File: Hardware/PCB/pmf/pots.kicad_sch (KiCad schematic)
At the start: 39 parts, among them U3 TL074, U4 TL072

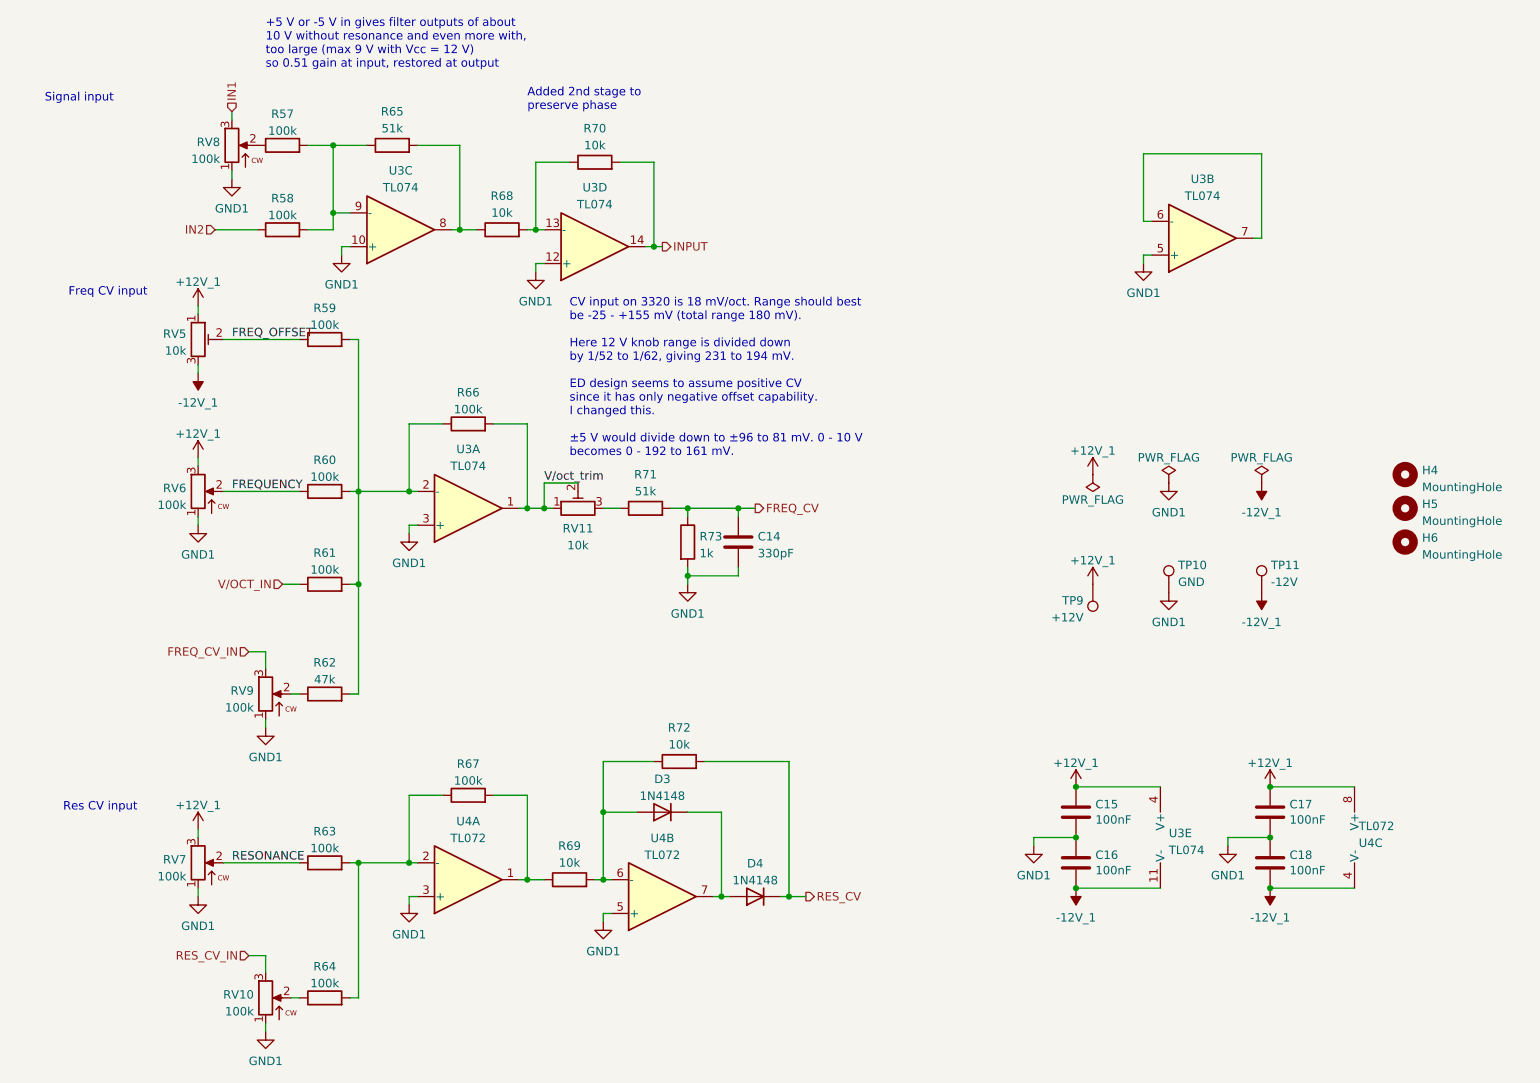
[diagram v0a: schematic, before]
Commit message: CVf test point; disambiguate heirarchical symbols
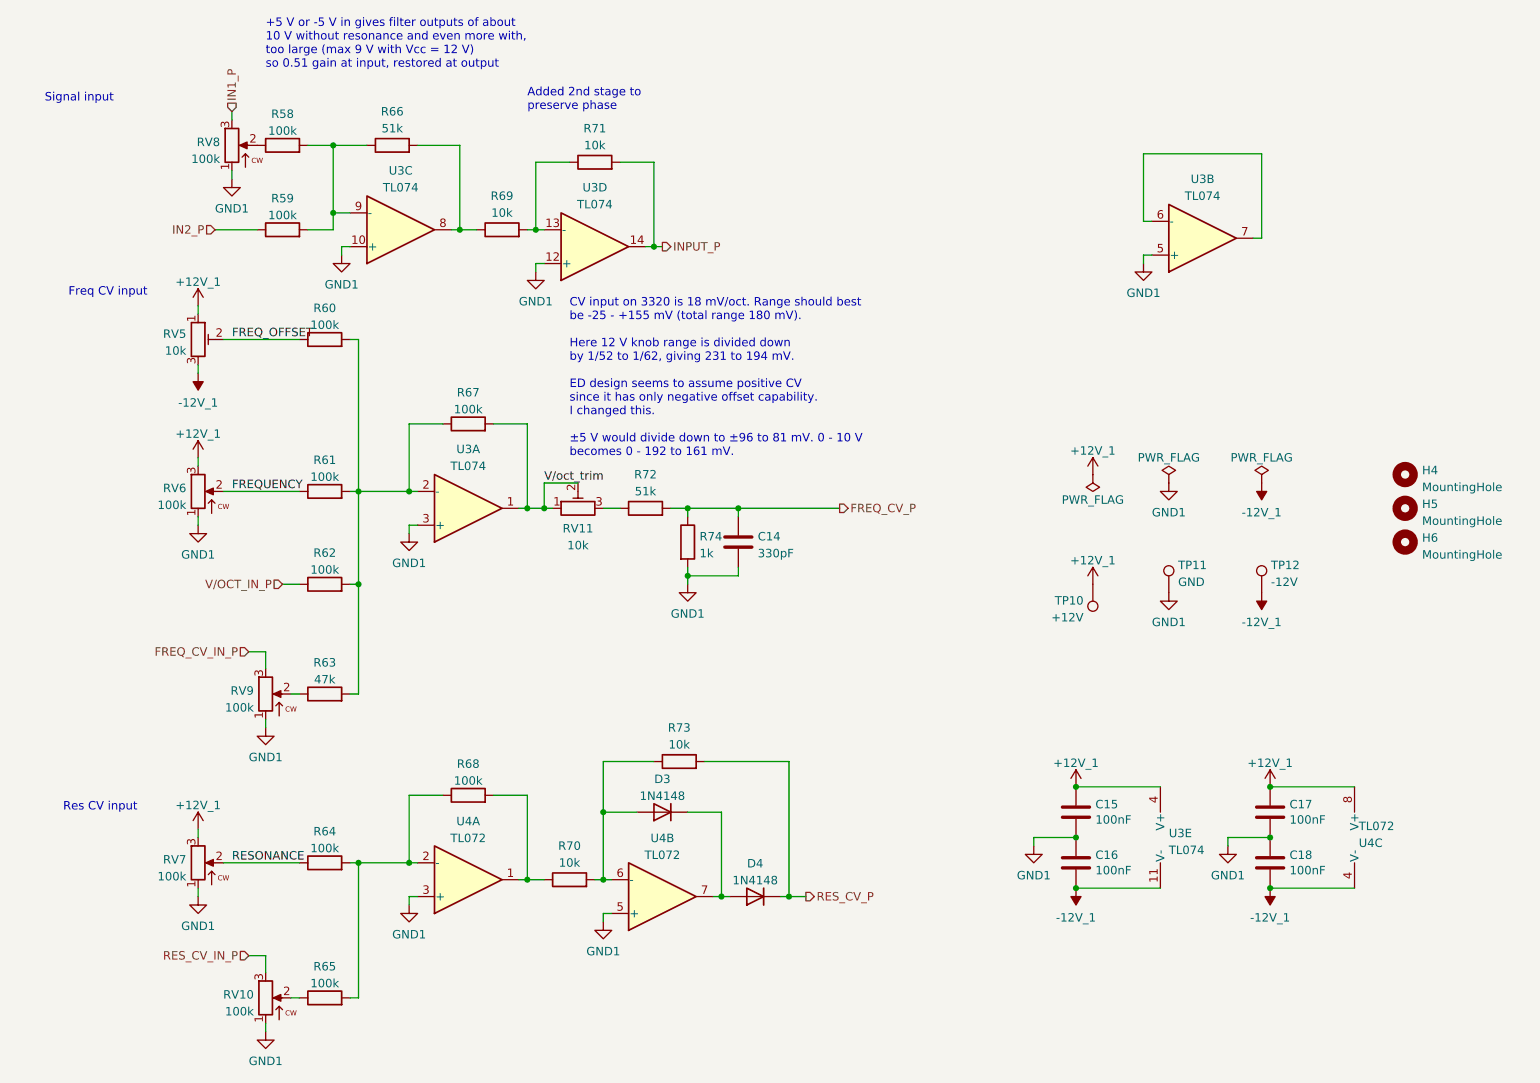
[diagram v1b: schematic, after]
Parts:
- renumbered R57 to R58, R58 to R59, R59 to R60, R60 to R61, R61 to R62, R62 to R63, R63 to R64, R64 to R65, R65 to R66, R66 to R67, R67 to R68, R68 to R69, R69 to R70, R70 to R71, R71 to R72, R72 to R73, R73 to R74, TP9 to TP10, TP10 to TP11, TP11 to TP12
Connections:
- net FREQ_CV renamed FREQ_CV_P
- net FREQ_CV_IN renamed FREQ_CV_IN_P
- net IN1 renamed IN1_P
- net IN2 renamed IN2_P
- net INPUT renamed INPUT_P
- net RES_CV renamed RES_CV_P
- net RES_CV_IN renamed RES_CV_IN_P
- net V/OCT_IN renamed V/OCT_IN_P

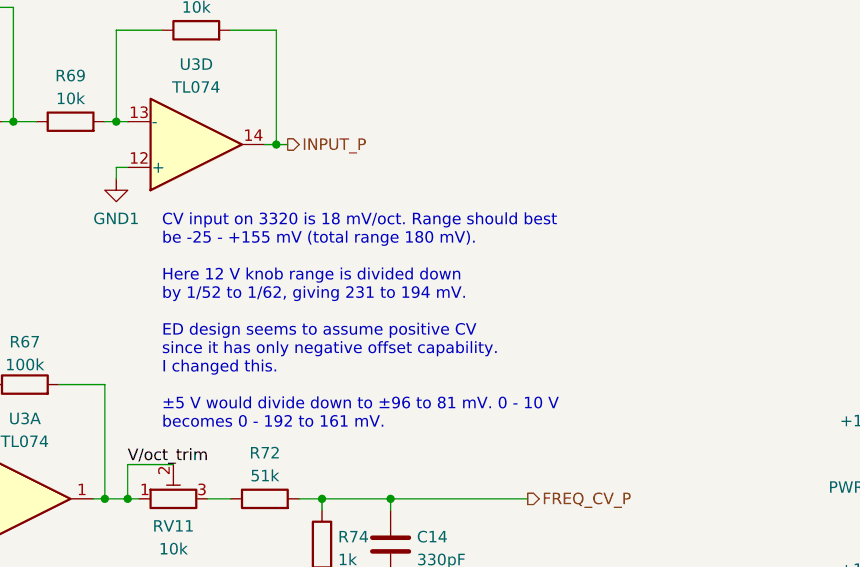
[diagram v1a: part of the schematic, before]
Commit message: Bigger trimmers for RC; slightly move expansion header
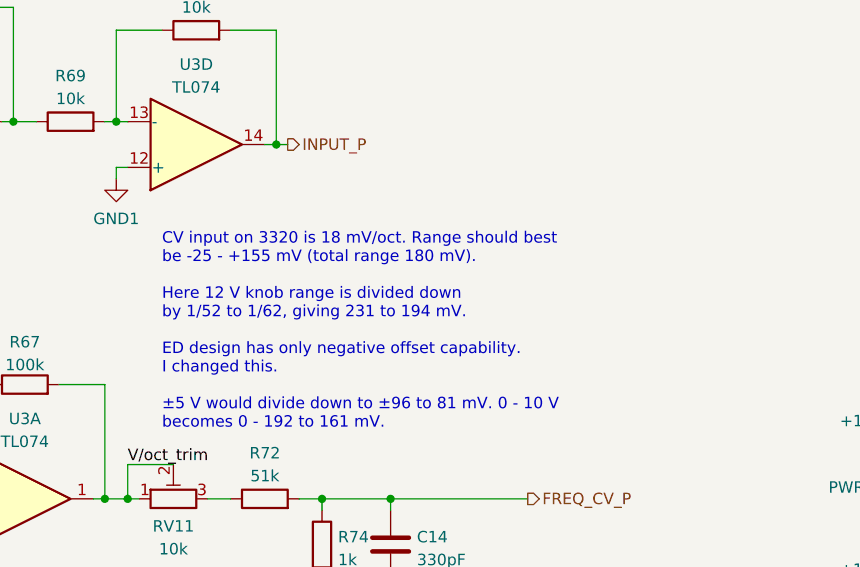
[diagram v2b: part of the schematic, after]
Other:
- note added: "CV input on 3320 is 18 mV/oct. Range should best be -25 - +155 mV (total range 180 mV). Here 12 V knob range is divided down by 1/52 to 1/62, giving 231 to 194 mV. ED design has only negative offset capability. I changed this. ±5 V would divide down to ±96 to 81 mV. 0 - 10 V becomes 0 - 192 to 161 mV."
- note removed: "CV input on 3320 is 18 mV/oct. Range should best be -25 - +155 mV (total range 180 mV). Here 12 V knob range is divided down by 1/52 to 1/62, giving 231 to 194 mV. ED design seems to assume positive CV since it has only negative offset capability. I changed this. ±5 V would divide down to ±96 to 81 mV. 0 - 10 V becomes 0 - 192 to 161 mV."
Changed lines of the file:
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@@
     (effects (font (size 1.27 1.27)) (justify left bottom))
   )
-  (text "CV input on 3320 is 18 mV/oct. Range should best \nbe -25 - +155 mV (total range 180 mV).\n\nHere 12 V knob range is divided down \nby 1/52 to 1/62, giving 231 to 194 mV.\n\nED design seems to assume positive CV \nsince it has only negative offset capability.\nI changed this.\n\n±5 V would divide down to ±96 to 81 mV. 0 - 10 V\nbecomes 0 - 192 to 161 mV."
+  (text "CV input on 3320 is 18 mV/oct. Range should best \nbe -25 - +155 mV (total range 180 mV).\n\nHere 12 V knob range is divided down \nby 1/52 to 1/62, giving 231 to 194 mV.\n\nED design has only negative offset capability.\nI changed this.\n\n±5 V would divide down to ±96 to 81 mV. 0 - 10 V\nbecomes 0 - 192 to 161 mV."
     (at 119.38 82.55 0)
     (effects (font (size 1.27 1.27)) (justify left bottom))

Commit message: Pre fab tweaks, Gerbers, BOM
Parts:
- added B2: Board, AO_tht:Board_Marker, symbol AO_symbols:Board
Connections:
- net +12V_1: now also RV5.3; no longer RV5.1
- net -12V_1: now also RV5.1; no longer RV5.3
- net V/oct_trim: now also RV11.3; no longer RV11.1
- net at R72.1: now also RV11.1; no longer RV11.3
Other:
- moved on the sheet: RV11

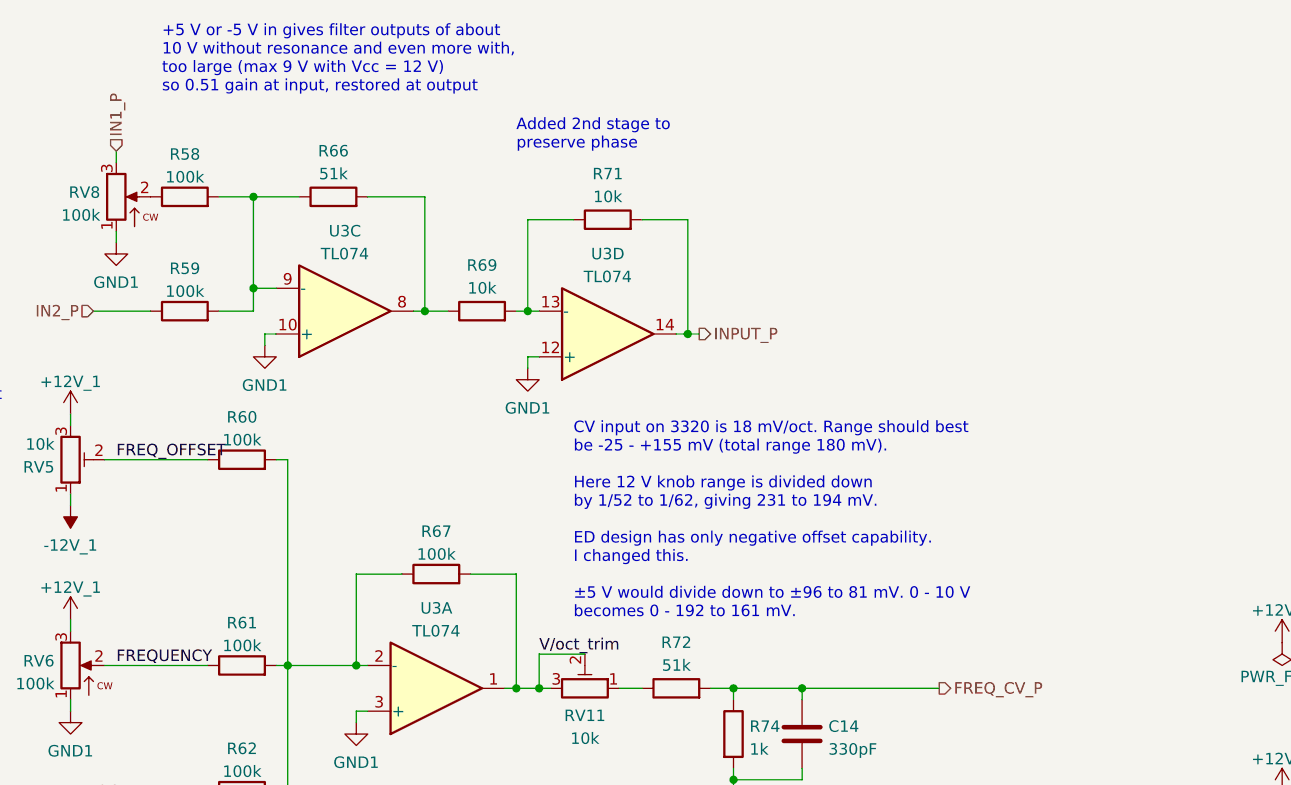
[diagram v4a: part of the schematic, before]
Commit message: Text boxes
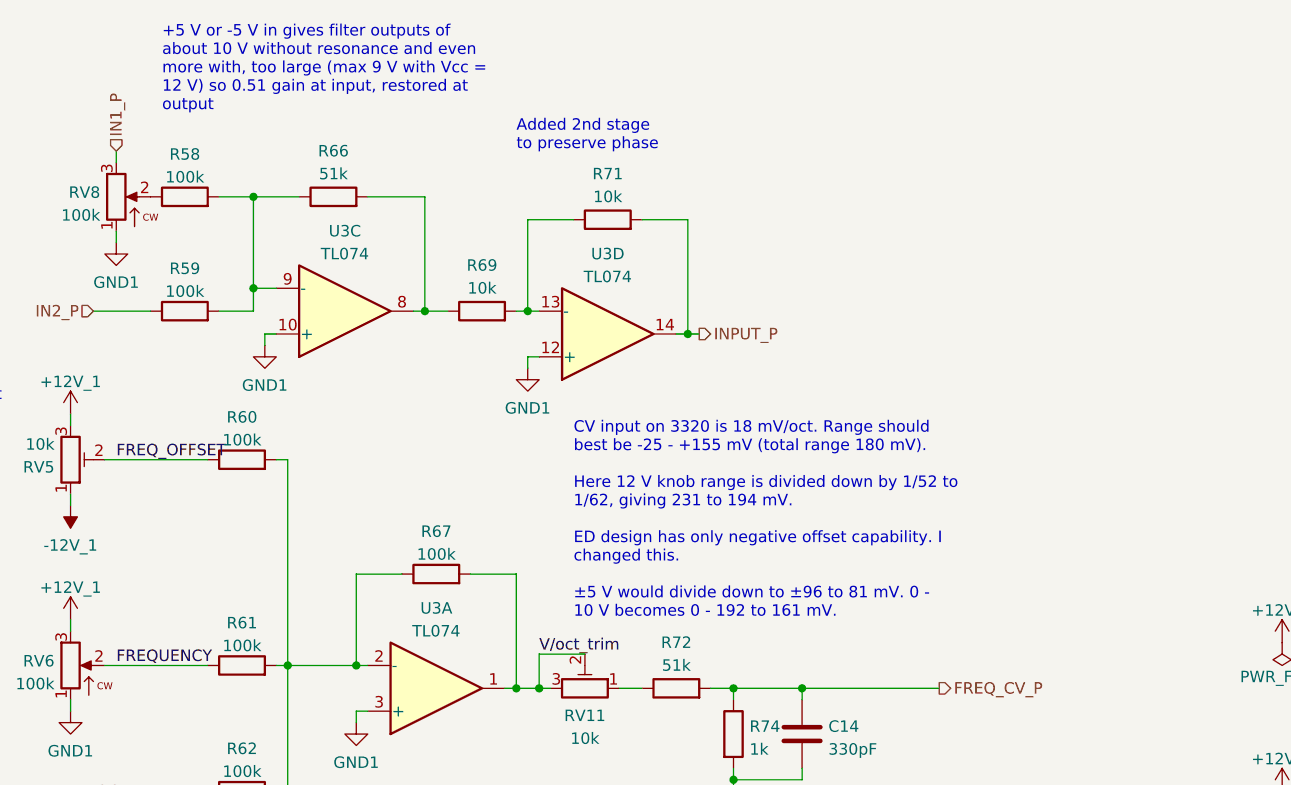
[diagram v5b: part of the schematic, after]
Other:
- note removed: "+5 V or -5 V in gives filter outputs of about 10 V without resonance and even more with, too large (max 9 V with Vcc = 12 V) so 0.51 gain at input, restored at output"
- note removed: "Added 2nd stage to preserve phase"
- note removed: "CV input on 3320 is 18 mV/oct. Range should best be -25 - +155 mV (total range 180 mV). Here 12 V knob range is divided down by 1/52 to 1/62, giving 231 to 194 mV. ED design has only negative offset capability. I changed this. ±5 V would divide down to ±96 to 81 mV. 0 - 10 V becomes 0 - 192 to 161 mV."
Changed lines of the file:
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@@
     (stroke (width 0) (type default))
   )
-  (text "Added 2nd stage to\npreserve phase" (at 113.03 30.48 0)
-    (effects (font (size 1.27 1.27)) (justify left bottom))
+  (text_box "+5 V or -5 V in gives filter outputs of about 10 V without resonance and even more with, too large (max 9 V with Vcc = 12 V) so 0.51 gain at input, restored at output"
+    (at 72.644 15.2748 0) (size 45.744 9.8712)
+    (stroke (width -0.0001) (type default))
+    (fill (type none))
+    (effects (font (size 1.27 1.27)) (justify left top))
   )
-  (text "CV input on 3320 is 18 mV/oct. Range should best \nbe -25 - +155 mV (total range 180 mV).\n\nHere 12 V knob range is divided down \nby 1/52 to 1/62, giving 231 to 194 mV.\n\nED design has only negative offset capability.\nI changed this.\n\n±5 V would divide down to ±96 to 81 mV. 0 - 10 V\nbecomes 0 - 192 to 161 mV."
-    (at 119.38 82.55 0)
-    (effects (font (size 1.27 1.27)) (justify left bottom))
+  (text_box "CV input on 3320 is 18 mV/oct. Range should best be -25 - +155 mV (total range 180 mV).\n\nHere 12 V knob range is divided down by 1/52 to 1/62, giving 231 to 194 mV.\n\nED design has only negative offset capability. I changed this.\n\n±5 V would divide down to ±96 to 81 mV. 0 - 10 V becomes 0 - 192 to 161 mV."
+    (at 118.364 59.293 0) (size 51.9366 24.273)
+    (stroke (width -0.0001) (type default))
+    (fill (type none))
+    (effects (font (size 1.27 1.27)) (justify left top))
   )
-  (text "+5 V or -5 V in gives filter outputs of about \n10 V without resonance and even more with, \ntoo large (max 9 V with Vcc = 12 V)\nso 0.51 gain at input, restored at output"
-    (at 73.66 24.13 0)
-    (effects (font (size 1.27 1.27)) (justify left bottom))
+  (text_box "Added 2nd stage to preserve phase"
+    (at 112.014 25.7396 0) (size 20.6586 5.7564)
+    (stroke (width -0.0001) (type default))
+    (fill (type none))
+    (effects (font (size 1.27 1.27)) (justify left top))
   )
   (text "Signal input" (at 50.8 29.21 0)
